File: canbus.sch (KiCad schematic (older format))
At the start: 16 parts, among them J601 Conn_01x04, J602 Conn_01x02, U601 RCLAMP0524P-N, U602 ISO1050DUB, U603 H7550-H#

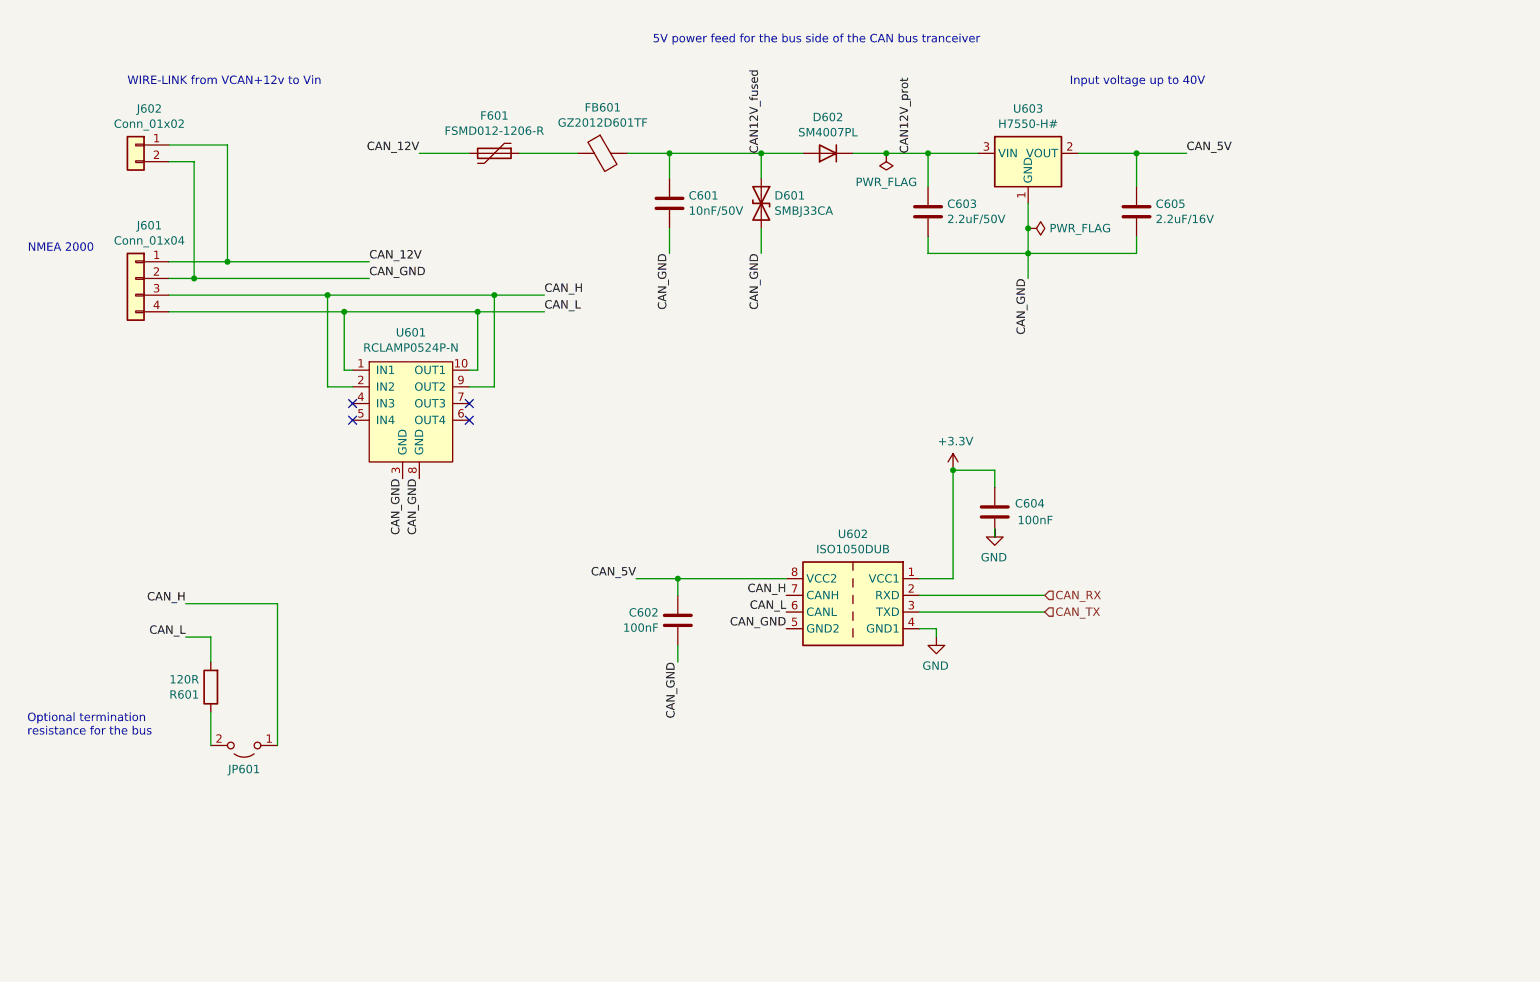
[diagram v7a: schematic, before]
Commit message: Use schottkys instead of MOSFETs for polarity protection
Also add a fuse to USB 5V and change the CAN terminator jumper
into a solder jumper.
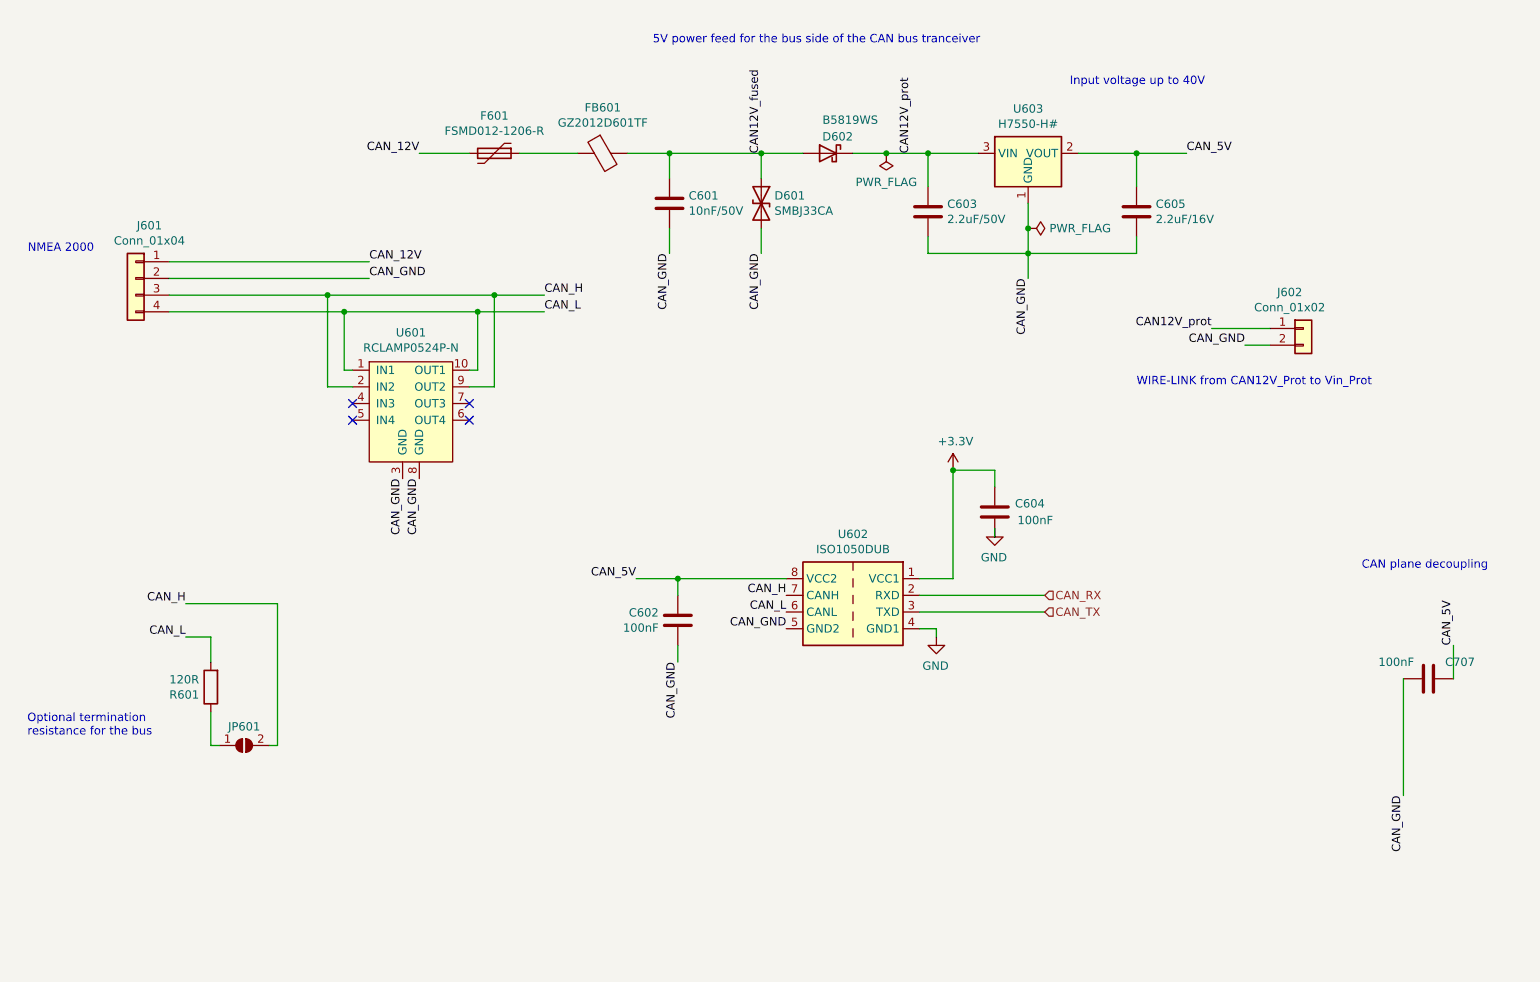
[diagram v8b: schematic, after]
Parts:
- removed D602: SM4007PL, Diode_SMD:D_SOD-123F, symbol Device:D
- removed JP601: Term, Connector_PinHeader_2.54mm:PinHeader_1x02_P2.54mm_Vertical, symbol Jumper:Jumper_2_Open
- added C707: 100nF, Capacitor_SMD:C_0402_1005Metric, symbol Device:C
- added D602: B5819WS, Diode_SMD:D_SOD-323F, symbol Device:D_Schottky
- added JP601: SolderJumper_2_Open, SH-ESP32:SolderJumper-2_P1.3mm_Open_TrianglePad_Narrow, symbol Jumper:SolderJumper_2_Open
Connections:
- net CAN12V_fused: now also D602.2 (A)
- net CAN12V_prot: now also J602.1 (Pin_1), D602.1 (K)
- net CAN_12V: no longer J602.1 (Pin_1)
- net CAN_5V: now also C707.1
- net CAN_GND: now also C707.2
- net CAN_H: now also JP601.2 (B)
- net at R601.1: now also JP601.1 (A)
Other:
- note added: "CAN plane decoupling"
- note added: "WIRE-LINK from CAN12V_Prot to Vin_Prot"
- note removed: "WIRE-LINK from VCAN+12v to Vin"
- moved on the sheet: J602
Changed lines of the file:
@@
 $Descr A4 11693 8268
 encoding utf-8
-Sheet 6 10
+Sheet 7 11
 Title "Sailor Hat for ESP32"
 Date ""
@@
 Wire Wire Line
 	1950 4350 2100 4350
-$Comp
-L Jumper:Jumper_2_Open JP601
-U 1 1 5C35395F
-P 2300 5000
-F 0 "JP601" H 2300 5143 50  0000 C CNN
-F 1 "Term" H 2300 5144 50  0001 C CNN
-F 2 "Connector_PinHeader_2.54mm:PinHeader_1x02_P2.54mm_Vertical" H 2300 5000 50  0001 C CNN
-F 3 "~" H 2300 5000 50  0001 C CNN
-F 4 "C376075" H 2300 5000 50  0001 C CNN "LCSC"
-	1    2300 5000
-	-1   0    0    1
-$EndComp
 $Comp
 L Device:R R601
@@
 	5950 1450 6150 1450
 $Comp
-L Device:D D?
-U 1 1 5F94C971
-P 5800 1450
-AR Path="/5C348474/5F94C971" Ref="D?"  Part="1"
-AR Path="/5E460E30/5F94C971" Ref="D?"  Part="1"
-AR Path="/5F6FAF6E/5F94C971" Ref="D?"  Part="1"
-AR Path="/5F733BA4/5F94C971" Ref="D602"  Part="1"
-F 0 "D602" H 5800 1234 50  0000 C CNN
-F 1 "SM4007PL" H 5800 1325 50  0000 C CNN
-F 2 "Diode_SMD:D_SOD-123F" H 5800 1450 50  0001 C CNN
-F 3 "~" H 5800 1450 50  0001 C CNN
-F 4 "C64898" H 5800 1450 50  0001 C CNN "LCSC"
-	1    5800 1450
-	-1   0    0    1
-$EndComp
-$Comp
 L Device:D_TVS D?
 U 1 1 5F94C96A
@@
 	1    0    0    -1
 $EndComp
-Wire Wire Line
-	1850 2100 2200 2100
 $Comp
 L SH-ESP32:RCLAMP0524P-N U601
@@
 Wire Wire Line
 	4850 1450 5400 1450
-Wire Wire Line
-	1850 2200 2000 2200
 Text Notes 1000 4950 0    50   ~ 0
 Optional termination\nresistance for the bus
@@
 L Connector_Generic:Conn_01x02 J?
 U 1 1 5FB62718
-P 1650 1400
+P 8650 2500
 AR Path="/5F6FAF6E/5FB62718" Ref="J?"  Part="1"
 AR Path="/5F733BA4/5FB62718" Ref="J602"  Part="1"
-F 0 "J602" H 1568 1617 50  0000 C CNN
-F 1 "Conn_01x02" H 1568 1526 50  0000 C CNN
-F 2 "SH-ESP32:WireLink_1x02_P2.54mm" H 1650 1400 50  0001 C CNN
-F 3 "~" H 1650 1400 50  0001 C CNN
-	1    1650 1400
-	-1   0    0    -1
-$EndComp
-Wire Wire Line
-	1850 1500 2000 1500
-Text Notes 1600 1050 0    50   ~ 0
-WIRE-LINK from VCAN+12v to Vin
-Wire Wire Line
-	1850 1400 2200 1400
-Wire Wire Line
-	2200 1400 2200 2100
-Connection ~ 2200 2100
-Wire Wire Line
-	2200 2100 3050 2100
-Wire Wire Line
-	2000 1500 2000 2200
-Connection ~ 2000 2200
-Wire Wire Line
-	2000 2200 3050 2200
+F 0 "J602" H 8568 2717 50  0000 C CNN
+F 1 "Conn_01x02" H 8568 2626 50  0000 C CNN
+F 2 "SH-ESP32:WireLink_1x02_P2.54mm" H 8650 2500 50  0001 C CNN
+F 3 "~" H 8650 2500 50  0001 C CNN
+	1    8650 2500
+	1    0    0    -1
+$EndComp
+Wire Wire Line
+	8450 2600 8300 2600
+Text Notes 7650 2850 0    50   ~ 0
+WIRE-LINK from CAN12V_Prot to Vin_Prot
+Wire Wire Line
+	8450 2500 8100 2500
+Wire Wire Line
+	1850 2100 3050 2100
+Wire Wire Line
+	1850 2200 3050 2200
+Text Label 8100 2500 2    50   ~ 0
+CAN12V_prot
+Text Label 8300 2600 2    50   ~ 0
+CAN_GND
+$Comp
+L Device:D_Schottky D?
+U 1 1 5FB60F25
+P 5800 1450
+AR Path="/5C3476D8/5FB60F25" Ref="D?"  Part="1"
+AR Path="/5CA65CC5/5FB60F25" Ref="D?"  Part="1"
+AR Path="/5F6FAF6E/5FB60F25" Ref="D?"  Part="1"
+AR Path="/5F733BA4/5FB60F25" Ref="D602"  Part="1"
+F 0 "D602" H 5650 1550 50  0000 L CNN
+F 1 "B5819WS" H 5500 1650 50  0000 L CNN
+F 2 "Diode_SMD:D_SOD-323F" H 5800 1450 50  0001 C CNN
+F 3 "~" H 5800 1450 50  0001 C CNN
+F 4 "" V 5800 1450 50  0001 C CNN "Notes"
+F 5 "C123899" H 5800 1450 50  0001 C CNN "LCSC"
+	1    5800 1450
+	-1   0    0    -1
+$EndComp
+$Comp
+L Jumper:SolderJumper_2_Open JP601
+U 1 1 5FB71E26
+P 2300 5000
+F 0 "JP601" H 2300 5113 50  0000 C CNN
+F 1 "SolderJumper_2_Open" H 2300 5114 50  0001 C CNN
+F 2 "SH-ESP32:SolderJumper-2_P1.3mm_Open_TrianglePad_Narrow" H 2300 5000 50  0001 C CNN
+F 3 "~" H 2300 5000 50  0001 C CNN
+	1    2300 5000
+	1    0    0    -1
+$EndComp
+Wire Wire Line
+	2150 5000 2100 5000
+Wire Wire Line
+	2450 5000 2500 5000
+$Comp
+L Device:C C?
+U 1 1 5FB9BEFB
+P 9400 4600
+AR Path="/5D6F1C7C/5FB9BEFB" Ref="C?"  Part="1"
+AR Path="/5C348474/5FB9BEFB" Ref="C?"  Part="1"
+AR Path="/5F733BA4/5FB9BEFB" Ref="C707"  Part="1"
+F 0 "C707" V 9500 4700 50  0000 L CNN
+F 1 "100nF" V 9500 4300 50  0000 L CNN
+F 2 "Capacitor_SMD:C_0402_1005Metric" H 9438 4450 50  0001 C CNN
+F 3 "~" H 9400 4600 50  0001 C CNN
+F 4 "C1525" H 9400 4600 50  0001 C CNN "LCSC"
+	1    9400 4600
+	0    1    -1   0
+$EndComp
+Text Label 9250 5300 3    50   ~ 0
+CAN_GND
+Text Label 9550 4400 1    50   ~ 0
+CAN_5V
+Wire Wire Line
+	9550 4400 9550 4600
+Wire Wire Line
+	9250 4600 9250 5300
+Text Notes 9000 3950 0    50   ~ 0
+CAN plane decoupling
 $EndSCHEMATC
